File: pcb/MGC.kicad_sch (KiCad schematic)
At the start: 73 parts, among them J1 USB_C_Receptacle, J10 Conn_01x04_Pin, J2 Conn_01x02_Pin, J3 103R012BB100, J4 Conn_02x03_Odd_Even, J5 Conn_02x05_Odd_Even, J6 Conn_01x04, J7 103R012BB100, J8 Conn_01x01_Pin, J9 Conn_01x01_Pin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

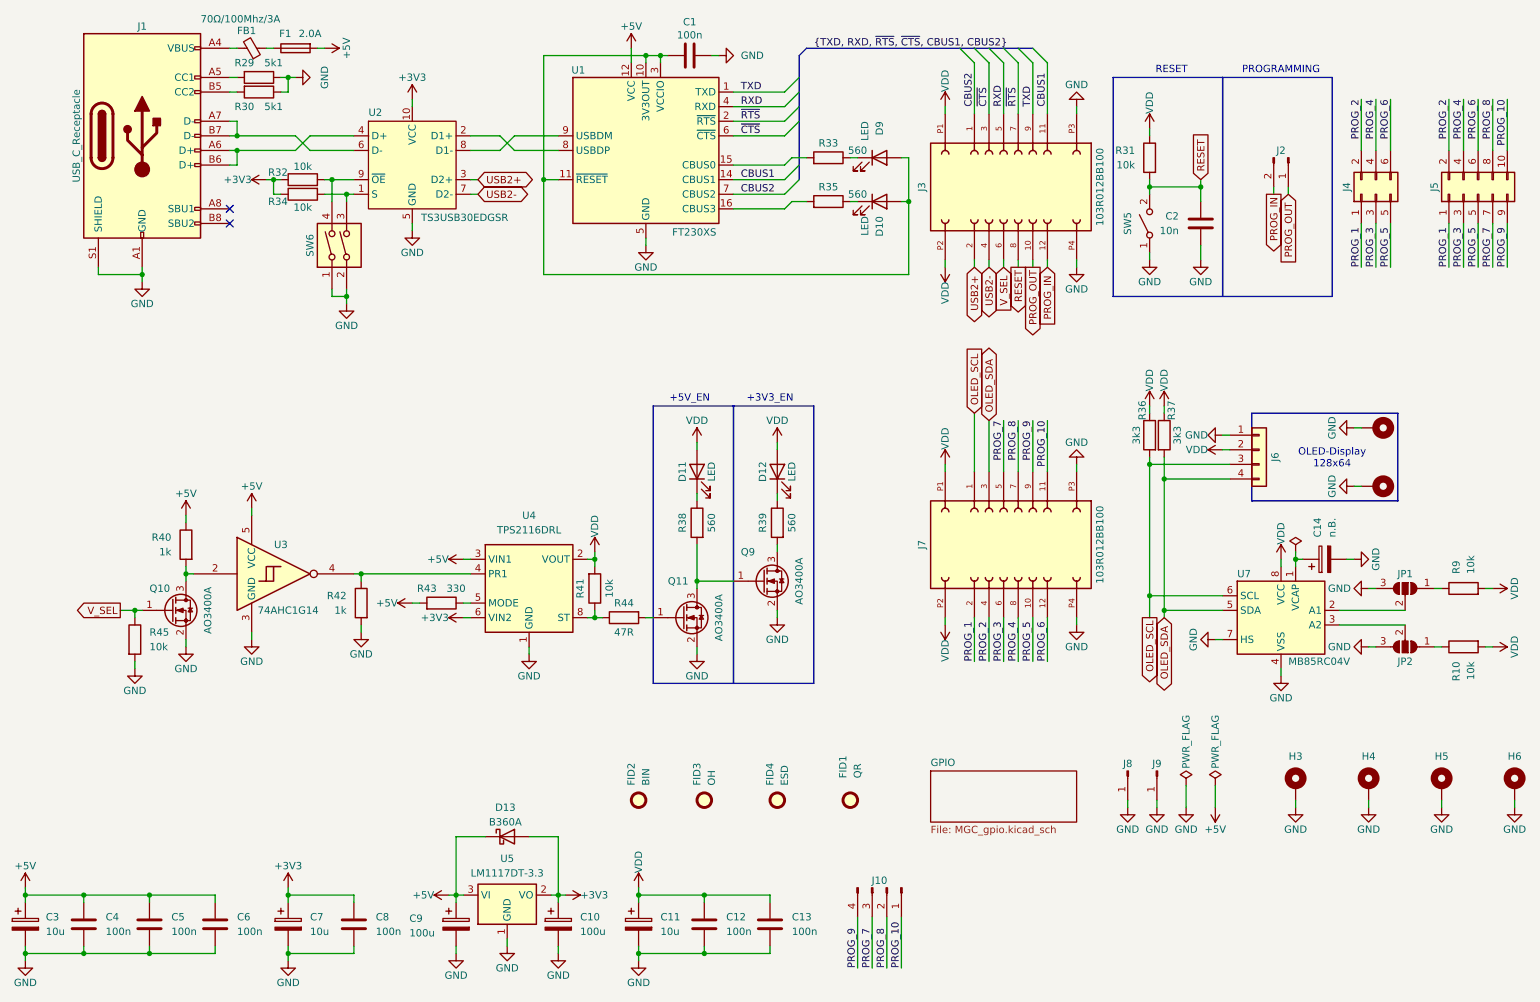
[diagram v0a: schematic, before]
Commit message: Adapt device values
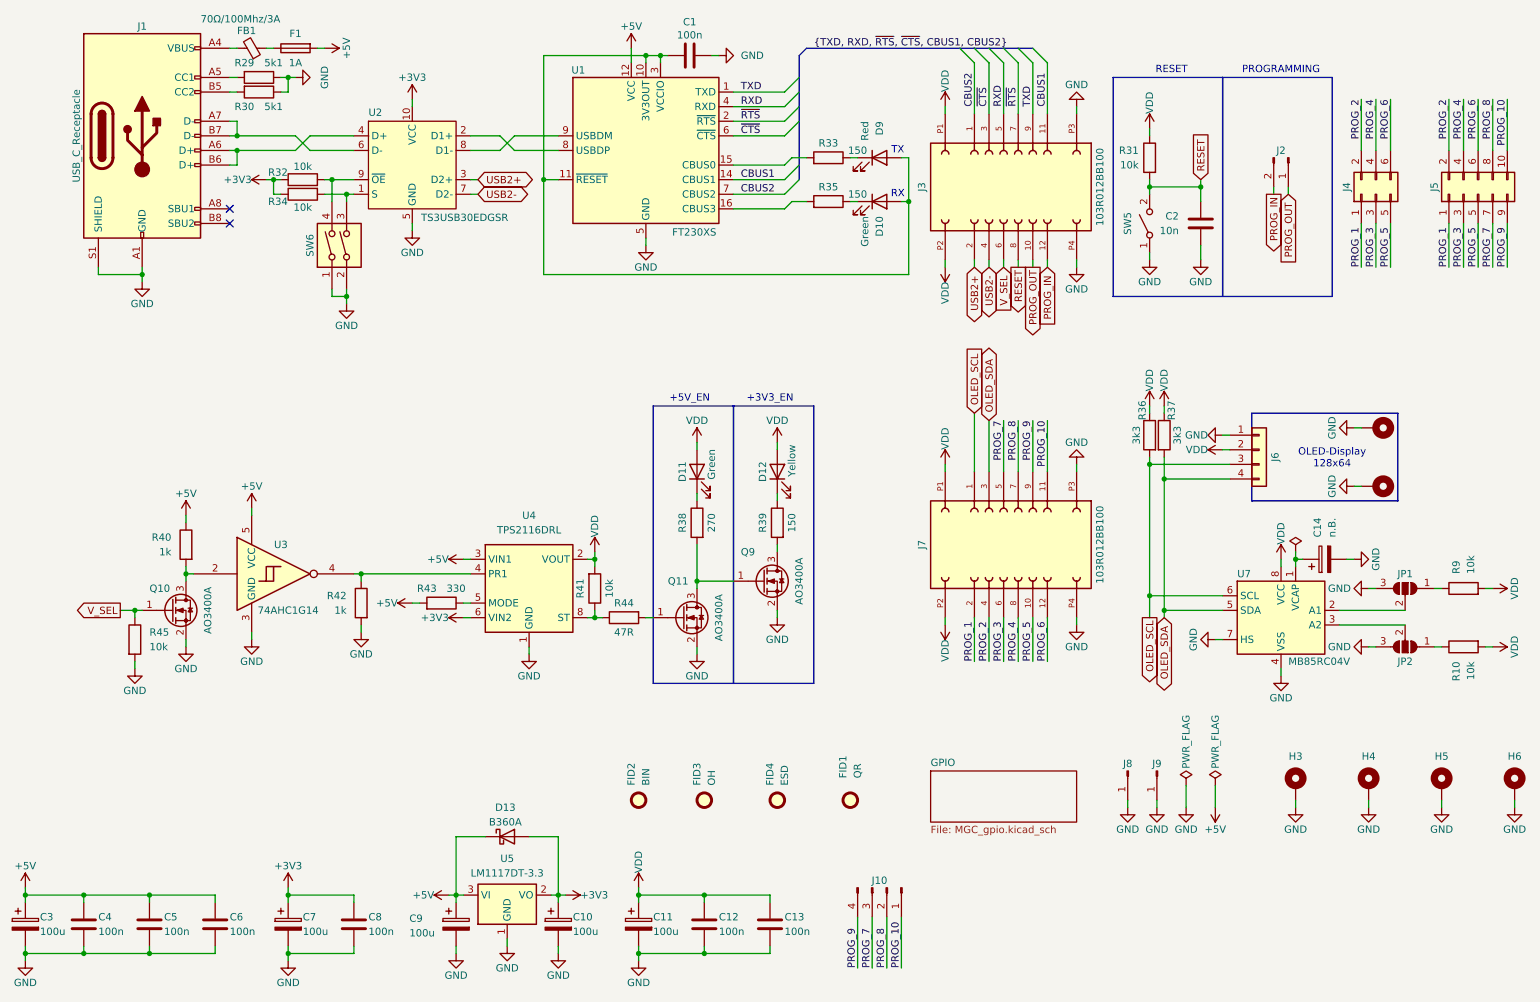
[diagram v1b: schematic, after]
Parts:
- C11, C3, C7: value 10u -> 100u
- D10, D11: value LED -> Green
- D12: value LED -> Yellow
- D9: value LED -> Red
- F1: value 2.0A -> 1A
- R33, R35, R39: value 560 -> 150
- R38: value 560 -> 270
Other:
- note added: "RX"
- note added: "TX"
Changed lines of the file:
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@@
 		)
 	)
+	(text "TX"
+		(exclude_from_sim no)
+		(at 172.085 43.18 0)
+		(effects
+			(font
+				(size 1.27 1.27)
+			)
+		)
+	)
 	(text "PROGRAMMING"
 		(exclude_from_sim no)
@@
 		)
 	)
+	(text "RX"
+		(exclude_from_sim no)
+		(at 172.085 50.8 0)
+		(effects
+			(font
+				(size 1.27 1.27)
+			)
+		)
+	)
 	(text "+3V3_EN"
 		(exclude_from_sim no)
@@
 			)
 		)
-		(property "Value" "LED"
-			(at 139.7 99.06 0)
+		(property "Value" "Green"
+			(at 139.7 97.79 0)
 			(effects
 				(font
@@
 			)
 		)
-		(property "Value" "LED"
+		(property "Value" "Red"
 			(at 166.37 38.1 90)
 			(effects
@@
 		(on_board yes)
 		(dnp no)
-		(fields_autoplaced yes)
 		(property "Reference" "C12"
-			(at 142.24 176.5299 0)
+			(at 140.97 176.5299 0)
 			(effects
 				(font
@@
 		)
 		(property "Value" "100n"
-			(at 142.24 179.0699 0)
+			(at 140.97 179.0699 0)
 			(effects
 				(font
@@
 		(dnp no)
 		(property "Reference" "C6"
-			(at 57.15 176.5299 0)
+			(at 55.88 176.53 0)
 			(effects
 				(font
@@
 		)
 		(property "Value" "100n"
-			(at 57.15 179.0699 0)
+			(at 55.88 179.07 0)
 			(effects
 				(font
@@
 			)
 		)
-		(property "Value" "LED"
+		(property "Value" "Green"
 			(at 166.37 54.61 90)
 			(effects
@@
 		(on_board yes)
 		(dnp no)
-		(fields_autoplaced yes)
 		(property "Reference" "C4"
-			(at 34.29 176.5299 0)
+			(at 33.02 176.53 0)
 			(effects
 				(font
@@
 		)
 		(property "Value" "100n"
-			(at 34.29 179.0699 0)
+			(at 33.02 179.07 0)
 			(effects
 				(font
@@
 		(on_board yes)
 		(dnp no)
-		(fields_autoplaced yes)
 		(property "Reference" "C5"
-			(at 45.72 176.5299 0)
+			(at 44.45 176.53 0)
 			(effects
 				(font
@@
 		)
 		(property "Value" "100n"
-			(at 45.72 179.0699 0)
+			(at 44.45 179.07 0)
 			(effects
 				(font
@@
 			)
 		)
-		(property "Value" "560"
+		(property "Value" "150"
 			(at 165.1 50.8 90)
 			(effects
@@
 		(on_board yes)
 		(dnp no)
-		(fields_autoplaced yes)
 		(property "Reference" "C8"
-			(at 81.28 176.5299 0)
+			(at 80.01 176.5299 0)
 			(effects
 				(font
@@
 		)
 		(property "Value" "100n"
-			(at 81.28 179.0699 0)
+			(at 80.01 179.0699 0)
 			(effects
 				(font
@@
 		(dnp no)
 		(property "Reference" "C11"
-			(at 130.81 176.53 0)
+			(at 129.54 176.53 0)
 			(effects
 				(font
@@
 			)
 		)
-		(property "Value" "10u"
-			(at 130.81 179.07 0)
+		(property "Value" "100u"
+			(at 129.54 179.07 0)
 			(effects
 				(font
@@
 		(dnp no)
 		(property "Reference" "C7"
-			(at 69.85 176.53 0)
+			(at 68.58 176.53 0)
 			(effects
 				(font
@@
 			)
 		)
-		(property "Value" "10u"
-			(at 69.85 179.07 0)
+		(property "Value" "100u"
+			(at 68.58 179.07 0)
 			(effects
 				(font
@@
 		(dnp no)
 		(property "Reference" "C10"
-			(at 116.84 176.53 0)
+			(at 115.57 176.53 0)
 			(effects
 				(font
@@
 		)
 		(property "Value" "100u"
-			(at 116.84 179.07 0)
+			(at 115.57 179.07 0)
 			(effects
 				(font
@@
 			)
 		)
-		(property "Value" "560"
+		(property "Value" "150"
 			(at 165.1 43.18 90)
 			(effects
@@
 			)
 		)
-		(property "Value" "560"
+		(property "Value" "270"
 			(at 139.7 107.95 90)
 			(effects
@@
 		(dnp no)
 		(property "Reference" "R31"
-			(at 213.36 43.1799 0)
+			(at 213.995 43.18 0)
 			(effects
 				(font
@@
 		)
 		(property "Value" "10k"
-			(at 213.36 45.7199 0)
+			(at 213.995 45.72 0)
 			(effects
 				(font
@@
 		(dnp no)
 		(property "Reference" "C3"
-			(at 23.876 176.53 0)
+			(at 22.86 176.53 0)
 			(effects
 				(font
@@
 			)
 		)
-		(property "Value" "10u"
-			(at 23.876 179.07 0)
+		(property "Value" "100u"
+			(at 22.86 179.07 0)
 			(effects
 				(font
@@
 		(on_board yes)
 		(dnp no)
-		(fields_autoplaced yes)
 		(property "Reference" "C13"
-			(at 153.67 176.5299 0)
+			(at 152.4 176.5299 0)
 			(effects
 				(font
@@
 		)
 		(property "Value" "100n"
-			(at 153.67 179.0699 0)
+			(at 152.4 179.0699 0)
 			(effects
 				(font
@@
 		(dnp no)
 		(property "Reference" "F1"
-			(at 65.532 22.86 90)
+			(at 67.31 22.86 90)
 			(effects
 				(font
@@
 			)
 		)
-		(property "Value" "2.0A"
-			(at 69.85 22.86 90)
+		(property "Value" "1A"
+			(at 67.31 27.94 90)
 			(effects
 				(font
@@
 			)
 		)
-		(property "Value" "560"
+		(property "Value" "150"
 			(at 153.67 107.95 90)
 			(effects
@@
 			)
 		)
-		(property "Value" "LED"
-			(at 153.67 99.06 0)
+		(property "Value" "Yellow"
+			(at 153.67 97.155 0)
 			(effects
 				(font

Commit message: Add missing vendor(id)
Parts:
- C1, C12, C13, C4, C5, C6, C8: HTL (none) -> 103250
- C10, C11, C3, C7: DigiKey (none) -> 478-3877-1-ND
- C2: HTL (none) -> 102538
- C9: value 100u -> 47u; HTL (none) -> 102856
- D10, D11: HTL (none) -> 100459
- D12: HTL (none) -> 100457
- D13: HTL (none) -> 103360
- D9: HTL (none) -> 100458
- F1: DigiKey (none) -> 5923-0ZCJ0100FF2ECT-ND; HTL 103597 -> (none)
- J10: DigiKey (none) -> S5596-ND
- J2: DigiKey (none) -> HDR100IMP40M-G-V-SM-ND
- J6, J8, J9: DigiKey (none) -> -; HTL (none) -> -
- Q10, Q11, Q9: value AO3400A -> AO3416; HTL (none) -> 103512
- R10, R31, R32, R34, R41, R45, R9: HTL (none) -> 102967
- R33, R35, R39: HTL (none) -> 102934
- R36, R37: HTL (none) -> 102959
- R38: HTL (none) -> 102938
- R40, R42: HTL (none) -> 102951
- R43: HTL (none) -> 102940
- R44: HTL (none) -> 102927
- SW5: HTL (none) -> 101613
- SW6: HTL (none) -> 103604
- U1: HTL (none) -> 103368
- U2: DigiKey (none) -> 296-25495-1-ND
- U3: HTL (none) -> 103595
- U4: DigiKey (none) -> 296-TPS2116DRLRCT-ND
- U5: HTL (none) -> 103444

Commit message: Fix connector pin direction
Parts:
- FID1: footprint Images:QR_0x007e_small -> Images:QR_0x007e_very_small
- J10: footprint Connector_PinSocket_2.54mm:PinSocket_1x04_P2.54mm_Vertical_SMD_Pin1Left -> Connector_PinSocket_2.54mm:PinSocket_1x04_P2.54mm_Vertical_SMD_Pin1Right
- J2: footprint Connector_PinHeader_2.54mm:PinHeader_1x02_P2.54mm_Vertical_SMD_Pin1Left -> Connector_PinHeader_2.54mm:PinHeader_1x02_P2.54mm_Vertical_SMD_Pin1Right
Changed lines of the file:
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@@
 			)
 		)
-		(property "Footprint" "Connector_PinSocket_2.54mm:PinSocket_1x04_P2.54mm_Vertical_SMD_Pin1Left"
+		(property "Footprint" "Connector_PinSocket_2.54mm:PinSocket_1x04_P2.54mm_Vertical_SMD_Pin1Right"
 			(at 170.18 171.45 0)
 			(effects
@@
 			)
 		)
-		(property "Footprint" "Connector_PinHeader_2.54mm:PinHeader_1x02_P2.54mm_Vertical_SMD_Pin1Left"
+		(property "Footprint" "Connector_PinHeader_2.54mm:PinHeader_1x02_P2.54mm_Vertical_SMD_Pin1Right"
 			(at 240.03 44.45 0)
 			(effects
@@
 			)
 		)
-		(property "Footprint" "Images:QR_0x007e_small"
+		(property "Footprint" "Images:QR_0x007e_very_small"
 			(at 163.83 156.21 0)
 			(effects

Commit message: Change reset capacitor device size
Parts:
- C2: footprint Capacitor_SMD:C_1206_3216Metric -> Capacitor_SMD:C_0603_1608Metric
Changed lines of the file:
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@@
 			)
 		)
-		(property "Footprint" "Capacitor_SMD:C_1206_3216Metric"
+		(property "Footprint" "Capacitor_SMD:C_0603_1608Metric"
 			(at 223.8248 59.69 0)
 			(effects
